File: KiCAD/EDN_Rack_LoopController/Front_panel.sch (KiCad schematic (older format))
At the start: 52 parts

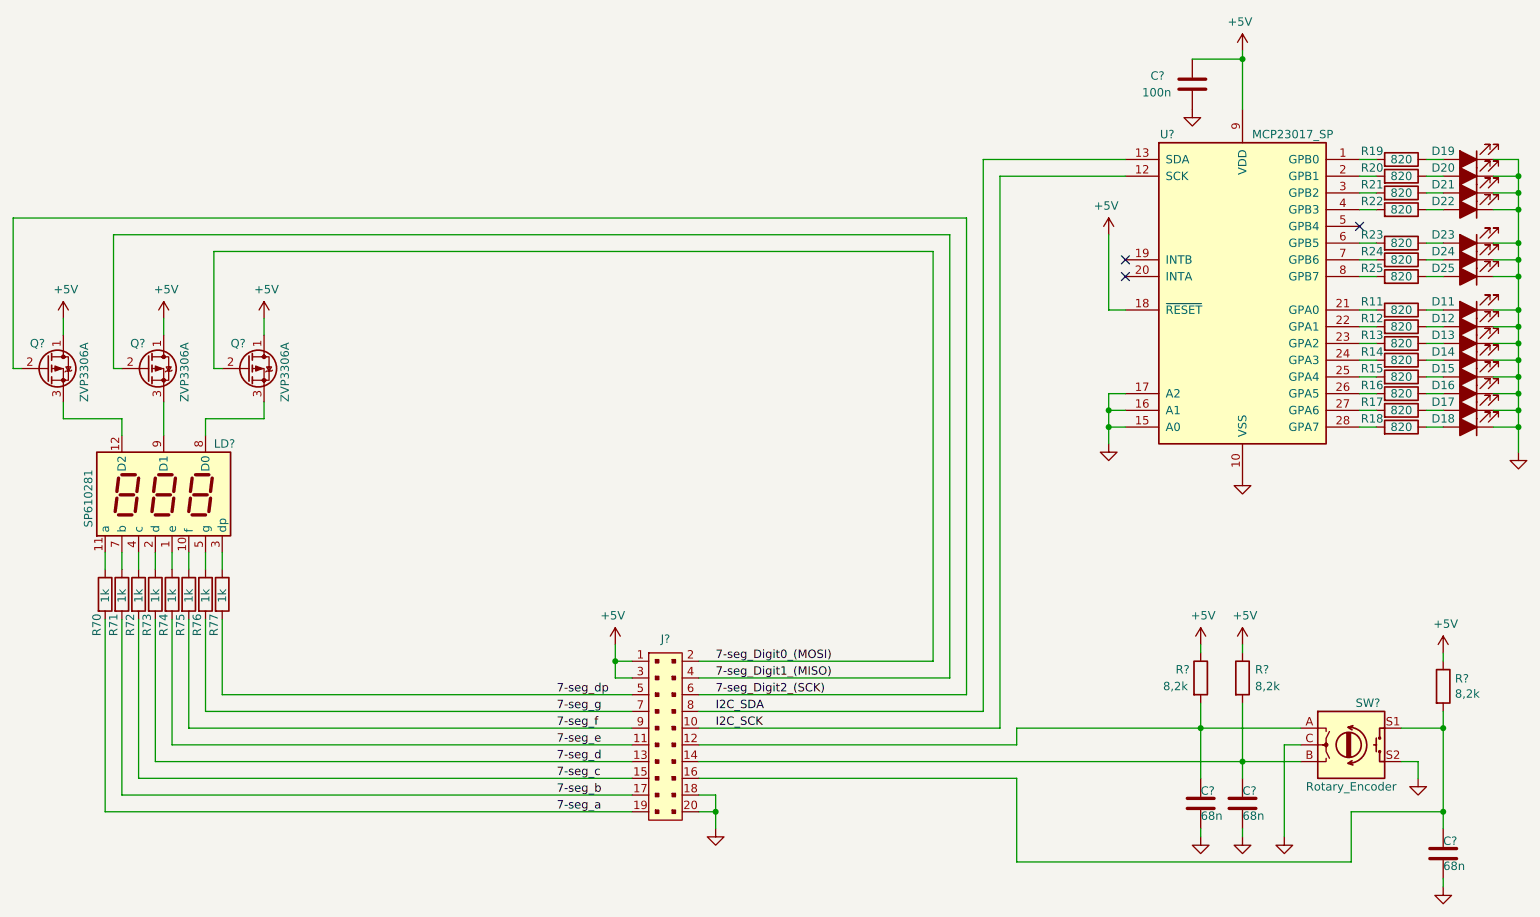
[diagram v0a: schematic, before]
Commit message: Schematic polish, added complete schematic pdf.
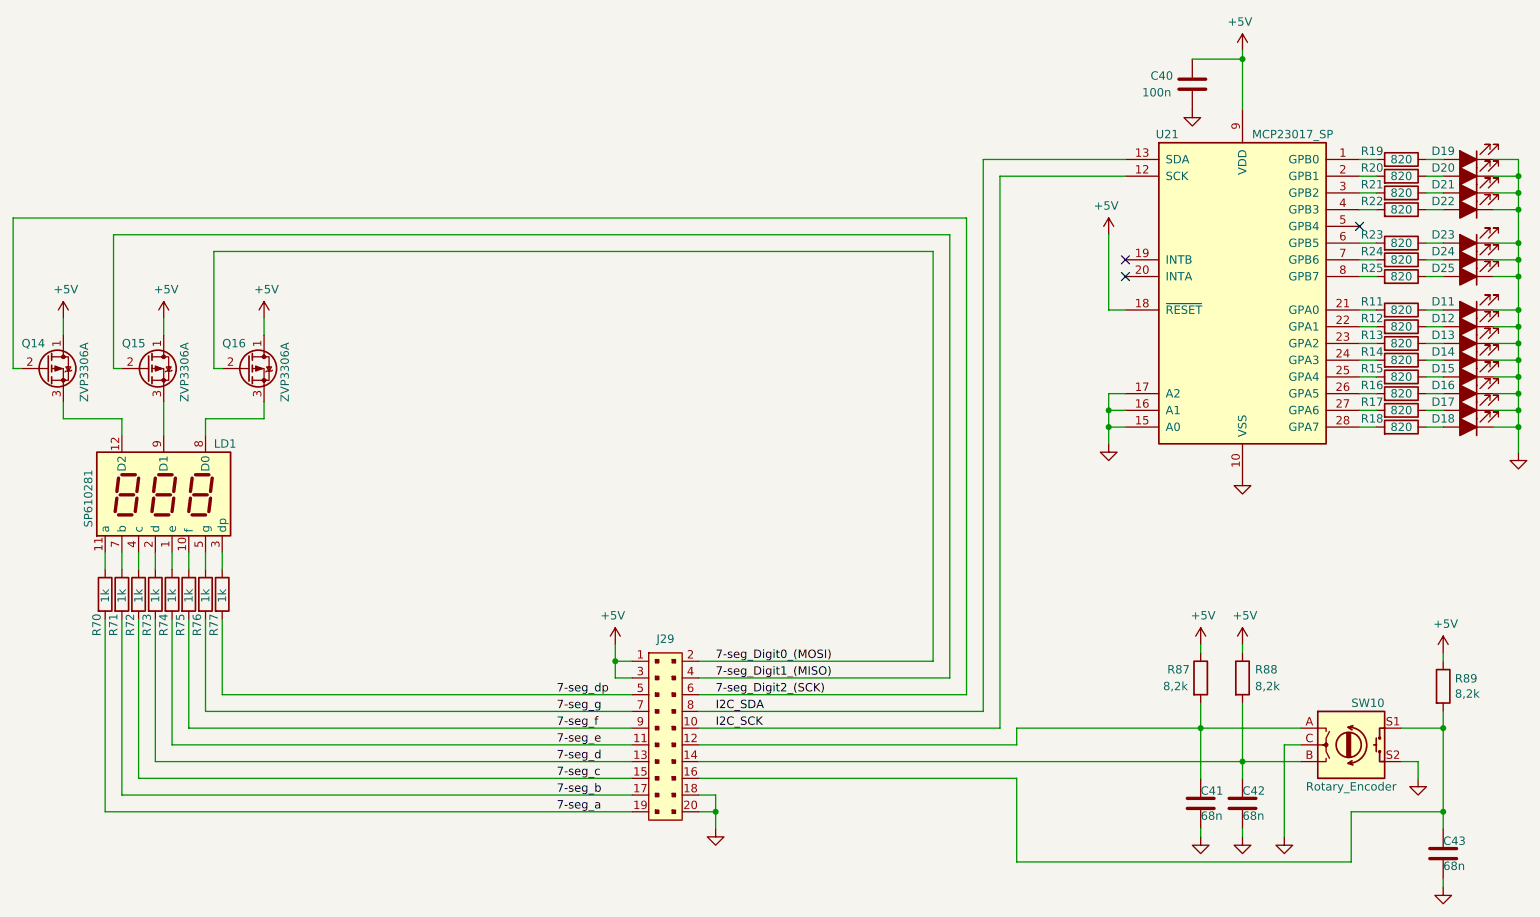
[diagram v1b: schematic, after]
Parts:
- gave numbers to parts that had none: 14
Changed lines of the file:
@@
 	7900 3300 7800 3300
 $Comp
-L power:GND #PWR?
+L power:GND #PWR0250
 U 1 1 5FE6A1CB
 P 7800 3400
-F 0 "#PWR?" H 7800 3150 50  0001 C CNN
+F 0 "#PWR0250" H 7800 3150 50  0001 C CNN
 F 1 "GND" H 7805 3227 50  0001 C CNN
 F 2 "" H 7800 3400 50  0001 C CNN
@@
 	10250 3300 10250 3450
 $Comp
-L power:GND #PWR?
+L power:GND #PWR0251
 U 1 1 5FE6A1CA
 P 10250 3450
-F 0 "#PWR?" H 10250 3200 50  0001 C CNN
+F 0 "#PWR0251" H 10250 3200 50  0001 C CNN
 F 1 "GND" H 10255 3277 50  0001 C CNN
 F 2 "" H 10250 3450 50  0001 C CNN
@@
 $EndComp
 $Comp
-L power:GND #PWR?
+L power:GND #PWR0252
 U 1 1 5F9B68F3
 P 8600 3600
-F 0 "#PWR?" H 8600 3350 50  0001 C CNN
+F 0 "#PWR0252" H 8600 3350 50  0001 C CNN
 F 1 "GND" H 8605 3427 50  0001 C CNN
 F 2 "" H 8600 3600 50  0001 C CNN
@@
 $EndComp
 $Comp
-L power:+5V #PWR?
+L power:+5V #PWR0253
 U 1 1 5E6A7731
 P 7800 2150
-F 0 "#PWR?" H 7800 2000 50  0001 C CNN
+F 0 "#PWR0253" H 7800 2000 50  0001 C CNN
 F 1 "+5V" H 7815 2323 50  0000 C CNN
 F 2 "" H 7800 2150 50  0001 C CNN
@@
 $EndComp
 $Comp
-L power:+5V #PWR?
+L power:+5V #PWR0254
 U 1 1 5F9B23A1
 P 8600 1050
-F 0 "#PWR?" H 8600 900 50  0001 C CNN
+F 0 "#PWR0254" H 8600 900 50  0001 C CNN
 F 1 "+5V" H 8615 1223 50  0000 C CNN
 F 2 "" H 8600 1050 50  0001 C CNN
@@
 $EndComp
 $Comp
-L Interface_Expansion:MCP23017_SP U?
+L Interface_Expansion:MCP23017_SP U21
 U 1 1 5E698594
 P 8600 2500
-F 0 "U?" H 8150 3450 50  0000 C CNN
+F 0 "U21" H 8150 3450 50  0000 C CNN
 F 1 "MCP23017_SP" H 8900 3450 50  0000 C CNN
 F 2 "Package_DIP:DIP-28_W7.62mm" H 8800 1500 50  0001 L CNN
@@
 $EndComp
 $Comp
-L Device:C C?
+L Device:C C40
 U 1 1 5F9B6932
 P 8300 1250
-F 0 "C?" H 8050 1300 50  0000 L CNN
+F 0 "C40" H 8050 1300 50  0000 L CNN
 F 1 "100n" H 8000 1200 50  0000 L CNN
 F 2 "" H 8338 1100 50  0001 C CNN
@@
 	8300 1100 8600 1100
 $Comp
-L power:GND #PWR?
+L power:GND #PWR0255
 U 1 1 5F9B2421
 P 8300 1400
-F 0 "#PWR?" H 8300 1150 50  0001 C CNN
+F 0 "#PWR0255" H 8300 1150 50  0001 C CNN
 F 1 "GND" H 8305 1227 50  0001 C CNN
 F 2 "" H 8300 1400 50  0001 C CNN
@@
 7-seg_Digit0_(MOSI)
 $Comp
-L EDN-symbol:SP610281 LD?
+L EDN-symbol:SP610281 LD1
 U 1 1 5EADC101
 P 2150 3700
-F 0 "LD?" H 2450 4000 50  0000 L CNN
+F 0 "LD1" H 2450 4000 50  0000 L CNN
 F 1 "SP610281" V 1700 3500 50  0000 L CNN
 F 2 "" V -860 3770 50  0001 C CNN
@@
 	1550 3150 1550 3250
 $Comp
-L power:+5V #PWR?
+L power:+5V #PWR0256
 U 1 1 5F9B691B
 P 2750 2650
-F 0 "#PWR?" H 2750 2500 50  0001 C CNN
+F 0 "#PWR0256" H 2750 2500 50  0001 C CNN
 F 1 "+5V" H 2765 2823 50  0000 C CNN
 F 2 "" H 2750 2650 50  0001 C CNN
@@
 $EndComp
 $Comp
-L power:+5V #PWR?
+L power:+5V #PWR0257
 U 1 1 5F9B23B8
 P 2150 2650
-F 0 "#PWR?" H 2150 2500 50  0001 C CNN
+F 0 "#PWR0257" H 2150 2500 50  0001 C CNN
 F 1 "+5V" H 2165 2823 50  0000 C CNN
 F 2 "" H 2150 2650 50  0001 C CNN
@@
 $EndComp
 $Comp
-L power:+5V #PWR?
+L power:+5V #PWR0258
 U 1 1 5F9B23B7
 P 1550 2650
-F 0 "#PWR?" H 1550 2500 50  0001 C CNN
+F 0 "#PWR0258" H 1550 2500 50  0001 C CNN
 F 1 "+5V" H 1565 2823 50  0000 C CNN
 F 2 "" H 1550 2650 50  0001 C CNN
@@
 $EndComp
 $Comp
-L EDN-symbol:ZVP3306A Q?
+L EDN-symbol:ZVP3306A Q16
 U 1 1 5F9B23B6
 P 2650 2950
-F 0 "Q?" H 2550 3100 50  0000 L CNN
+F 0 "Q16" H 2500 3100 50  0000 L CNN
 F 1 "ZVP3306A" V 2875 2750 50  0000 L CNN
 F 2 "Package_TO_SOT_THT:TO-92Flat" H 3450 2950 50  0001 C CIN
@@
 $EndComp
 $Comp
-L EDN-symbol:ZVP3306A Q?
+L EDN-symbol:ZVP3306A Q15
 U 1 1 5FE6A1CD
 P 2050 2950
-F 0 "Q?" H 1950 3100 50  0000 L CNN
+F 0 "Q15" H 1900 3100 50  0000 L CNN
 F 1 "ZVP3306A" V 2275 2750 50  0000 L CNN
 F 2 "Package_TO_SOT_THT:TO-92Flat" H 2850 2950 50  0001 C CIN
@@
 $EndComp
 $Comp
-L EDN-symbol:ZVP3306A Q?
+L EDN-symbol:ZVP3306A Q14
 U 1 1 5FE6A1CC
 P 1450 2950
-F 0 "Q?" H 1350 3100 50  0000 L CNN
+F 0 "Q14" H 1300 3100 50  0000 L CNN
 F 1 "ZVP3306A" V 1675 2750 50  0000 L CNN
 F 2 "Package_TO_SOT_THT:TO-92Flat" H 2250 2950 50  0001 C CIN
@@
 $EndComp
 $Comp
-L EDN-symbol:302-S201 J?
+L EDN-symbol:302-S201 J29
 U 1 1 5F9A2607
 P 5150 5150
-F 0 "J?" H 5150 5733 50  0000 C CNN
+F 0 "J29" H 5150 5733 50  0000 C CNN
 F 1 "302-S201" H 5150 5734 50  0001 C CNN
 F 2 "" H 5350 5600 60  0001 L CNN
@@
 	4950 4900 2500 4900
 $Comp
-L power:GND #PWR?
+L power:GND #PWR0259
 U 1 1 5FBC4C63
 P 5450 5700
-F 0 "#PWR?" H 5450 5450 50  0001 C CNN
+F 0 "#PWR0259" H 5450 5450 50  0001 C CNN
 F 1 "GND" H 5455 5527 50  0001 C CNN
 F 2 "" H 5450 5700 50  0001 C CNN
@@
 	5450 5600 5350 5600
 $Comp
-L power:+5V #PWR?
+L power:+5V #PWR0260
 U 1 1 5FBCDD57
 P 4850 4600
-F 0 "#PWR?" H 4850 4450 50  0001 C CNN
+F 0 "#PWR0260" H 4850 4450 50  0001 C CNN
 F 1 "+5V" H 4865 4773 50  0000 C CNN
 F 2 "" H 4850 4600 50  0001 C CNN
@@
 	8950 5100 8350 5100
 $Comp
-L Device:Rotary_Encoder_Switch SW?
+L Device:Rotary_Encoder_Switch SW10
 U 1 1 5F9B23BF
 P 9250 5200
-F 0 "SW?" H 9350 5450 50  0000 C CNN
+F 0 "SW10" H 9350 5450 50  0000 C CNN
 F 1 "Rotary_Encoder" H 9250 4950 50  0000 C CNN
 F 2 "" H 9100 5360 50  0001 C CNN
@@
 $EndComp
 $Comp
-L power:GND #PWR?
+L power:GND #PWR0261
 U 1 1 5F9B23C0
 P 9650 5400
-F 0 "#PWR?" H 9650 5150 50  0001 C CNN
+F 0 "#PWR0261" H 9650 5150 50  0001 C CNN
 F 1 "GND" H 9655 5227 50  0001 C CNN
 F 2 "" H 9650 5400 50  0001 C CNN
@@
 	9650 5300 9550 5300
 $Comp
-L power:GND #PWR?
+L power:GND #PWR0262
 U 1 1 5F9B6924
 P 8850 5750
-F 0 "#PWR?" H 8850 5500 50  0001 C CNN
+F 0 "#PWR0262" H 8850 5500 50  0001 C CNN
 F 1 "GND" H 8855 5577 50  0001 C CNN
 F 2 "" H 8850 5750 50  0001 C CNN
@@
 	8950 5200 8850 5200
 $Comp
-L Device:R R?
+L Device:R R87
 U 1 1 5F9B6925
 P 8350 4800
-F 0 "R?" H 8200 4850 50  0000 L CNN
+F 0 "R87" H 8150 4850 50  0000 L CNN
 F 1 "8,2k" H 8125 4750 50  0000 L CNN
 F 2 "" V 8280 4800 50  0001 C CNN
@@
 $EndComp
 $Comp
-L Device:R R?
+L Device:R R88
 U 1 1 5F9B6926
 P 8600 4800
-F 0 "R?" H 8675 4850 50  0000 L CNN
+F 0 "R88" H 8675 4850 50  0000 L CNN
 F 1 "8,2k" H 8675 4750 50  0000 L CNN
 F 2 "" V 8530 4800 50  0001 C CNN
@@
 $EndComp
 $Comp
-L Device:R R?
+L Device:R R89
 U 1 1 5F9B23C1
 P 9800 4850
-F 0 "R?" H 9870 4896 50  0000 L CNN
+F 0 "R89" H 9870 4896 50  0000 L CNN
 F 1 "8,2k" H 9870 4805 50  0000 L CNN
 F 2 "" V 9730 4850 50  0001 C CNN
@@
 $EndComp
 $Comp
-L power:+5V #PWR?
+L power:+5V #PWR0263
 U 1 1 5FE6A1D0
 P 8600 4600
-F 0 "#PWR?" H 8600 4450 50  0001 C CNN
+F 0 "#PWR0263" H 8600 4450 50  0001 C CNN
 F 1 "+5V" H 8615 4773 50  0000 C CNN
 F 2 "" H 8600 4600 50  0001 C CNN
@@
 $EndComp
 $Comp
-L power:+5V #PWR?
+L power:+5V #PWR0264
 U 1 1 5E884A44
 P 8350 4600
-F 0 "#PWR?" H 8350 4450 50  0001 C CNN
+F 0 "#PWR0264" H 8350 4450 50  0001 C CNN
 F 1 "+5V" H 8365 4773 50  0000 C CNN
 F 2 "" H 8350 4600 50  0001 C CNN
@@
 $EndComp
 $Comp
-L power:+5V #PWR?
+L power:+5V #PWR0265
 U 1 1 5E884E07
 P 9800 4650
-F 0 "#PWR?" H 9800 4500 50  0001 C CNN
+F 0 "#PWR0265" H 9800 4500 50  0001 C CNN
 F 1 "+5V" H 9815 4823 50  0000 C CNN
 F 2 "" H 9800 4650 50  0001 C CNN
@@
 	8350 4650 8350 4600
 $Comp
-L Device:C C?
+L Device:C C42
 U 1 1 5E89884B
 P 8600 5550
-F 0 "C?" H 8600 5625 50  0000 L CNN
+F 0 "C42" H 8600 5625 50  0000 L CNN
 F 1 "68n" H 8600 5475 50  0000 L CNN
 F 2 "" H 8638 5400 50  0001 C CNN
@@
 $EndComp
 $Comp
-L power:GND #PWR?
+L power:GND #PWR0266
 U 1 1 5F9B692C
 P 8600 5750
-F 0 "#PWR?" H 8600 5500 50  0001 C CNN
+F 0 "#PWR0266" H 8600 5500 50  0001 C CNN
 F 1 "GND" H 8605 5577 50  0001 C CNN
 F 2 "" H 8600 5750 50  0001 C CNN
@@
 	8850 5200 8850 5750
 $Comp
-L Device:C C?
+L Device:C C41
 U 1 1 5FE6A1D4
 P 8350 5550
-F 0 "C?" H 8350 5625 50  0000 L CNN
+F 0 "C41" H 8350 5625 50  0000 L CNN
 F 1 "68n" H 8350 5475 50  0000 L CNN
 F 2 "" H 8388 5400 50  0001 C CNN
@@
 $EndComp
 $Comp
-L power:GND #PWR?
+L power:GND #PWR0267
 U 1 1 5FE6A1D5
 P 8350 5750
-F 0 "#PWR?" H 8350 5500 50  0001 C CNN
+F 0 "#PWR0267" H 8350 5500 50  0001 C CNN
 F 1 "GND" H 8355 5577 50  0001 C CNN
 F 2 "" H 8350 5750 50  0001 C CNN
@@
 	9800 5000 9800 5100
 $Comp
-L Device:C C?
+L Device:C C43
 U 1 1 5F9B692F
 P 9800 5850
-F 0 "C?" H 9800 5925 50  0000 L CNN
+F 0 "C43" H 9800 5925 50  0000 L CNN
 F 1 "68n" H 9800 5775 50  0000 L CNN
 F 2 "" H 9838 5700 50  0001 C CNN
@@
 	9250 5600 9250 5900
 $Comp
-L power:GND #PWR?
+L power:GND #PWR0268
 U 1 1 5F9B6930
 P 9800 6050
-F 0 "#PWR?" H 9800 5800 50  0001 C CNN
+F 0 "#PWR0268" H 9800 5800 50  0001 C CNN
 F 1 "GND" H 9805 5877 50  0001 C CNN
 F 2 "" H 9800 6050 50  0001 C CNN
